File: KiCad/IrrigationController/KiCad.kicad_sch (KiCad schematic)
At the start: 117 parts, among them IC1 MCP23017-E_SO, IC2 MCP23017-E_SO, IC3 DS89C21TMX_NOPB, J1 Screw_Terminal_01x03, J10 Screw_Terminal_01x05, J11 Screw_Terminal_01x02, J12 Screw_Terminal_01x02, J13 Screw_Terminal_01x04, J14 Screw_Terminal_01x02, J15 Screw_Terminal_01x02, J16 Screw_Terminal_01x02, J17 Screw_Terminal_01x02, J18 Screw_Terminal_01x02, J19 Screw_Terminal_01x02, J2 Screw_Terminal_01x03, J20 Conn_01x03_Pin, J21 Screw_Terminal_01x06, J22 Conn_01x04_Pin, J23 Conn_01x05_Pin, J24 Conn_01x06_Pin, J3 Screw_Terminal_01x03, J4 Conn_01x02_Pin, J5 Screw_Terminal_01x03, J6 Screw_Terminal_01x02, J7 Screw_Terminal_01x02, J8 Screw_Terminal_01x02, J9 Screw_Terminal_01x02, K1 2071556-9, K2 2071556-9, Q1 MMBT3906, Q11 MMBT3904, Q12 MMBT3904, Q2 MMBT3906, Q3 MMBT3906, Q6 MMBT3904, Q7 MMBT3904, Q8 MMBT3904, SW1 SW_Push, U1 L298P, U2 ARDUINO_MKR_WAN_1310, U3 L298P, U4 L298P, U5 L298P, U7 L7805

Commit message: Añadido C15 al esquema, que se había esfumado
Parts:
- added C15: 0.1u, Capacitor_SMD:C_1206_3216Metric, symbol Device:C
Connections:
- net +3.3V: now also C15.1
- net Earth: now also C15.2
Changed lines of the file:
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@@
 	)
 	(junction
+		(at 261.62 20.32)
+		(diameter 0)
+		(color 0 0 0 0)
+	)
+	(junction
 		(at 102.87 152.4)
 		(diameter 0)
@@
 	)
 	(junction
+		(at 261.62 27.94)
+		(diameter 0)
+		(color 0 0 0 0)
+	)
+	(junction
 		(at 119.38 185.42)
 		(diameter 0)
@@
 	(wire
 		(pts
+			(xy 254 20.32) (xy 261.62 20.32)
+		)
+		(stroke
+			(width 0)
+			(type default)
+		)
+	)
+	(wire
+		(pts
 			(xy 144.78 152.4) (xy 143.51 152.4)
 		)
@@
 	(wire
 		(pts
+			(xy 254 27.94) (xy 261.62 27.94)
+		)
+		(stroke
+			(width 0)
+			(type default)
+		)
+	)
+	(wire
+		(pts
 			(xy 168.91 149.86) (xy 170.18 149.86)
 		)
@@
 					(unit 1)
 				)
+			)
+		)
+	)
+	(symbol
+		(lib_id "Device:C")
+		(at 254 24.13 0)
+		(unit 1)
+		(exclude_from_sim no)
+		(in_bom yes)
+		(on_board yes)
+		(dnp no)
+		(property "Reference" "C15"
+			(at 256.54 26.67 0)
+			(effects
+				(font
+					(size 1.27 1.27)
+				)
+			)
+		)
+		(property "Value" "0.1u"
+			(at 250.19 21.59 0)
+			(effects
+				(font
+					(size 1.27 1.27)
+				)
+			)
+		)
+		(property "Footprint" "Capacitor_SMD:C_1206_3216Metric"
+			(at 254.9652 27.94 0)
+			(effects
+				(font
+					(size 1.27 1.27)
+				)
+				(hide yes)
+			)
+		)
+		(property "Datasheet" "~"
+			(at 254 24.13 0)
+			(effects
+				(font
+					(size 1.27 1.27)
+				)
+				(hide yes)
+			)
+		)
+		(property "Description" ""
+			(at 254 24.13 0)
+			(effects
+				(font
+					(size 1.27 1.27)
+				)
+				(hide yes)
+			)
+		)
+		(property "Mouser Part Number" "80-C1206X104K1RAUTO"
+			(at 254 24.13 0)
+			(effects
+				(font
+					(size 1.27 1.27)
+				)
+				(hide yes)
+			)
+		)
+		(pin "1"
+		)
+		(pin "2"
+		)
+		(instances
+			(project "KiCad"
+				(path "/557850ac-a946-4dff-8187-8978353577df"
+					(reference "C15")
+					(unit 1)
+				)

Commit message: fixed error on I2C lines
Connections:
- net SCL: now also IC1.12 (SCL), IC2.12 (SCL), J13.2 (Pin_2); no longer IC1.13 (SDA), IC2.13 (SDA), J13.3 (Pin_3)
- net SDA: now also IC1.13 (SDA), IC2.13 (SDA), J13.3 (Pin_3); no longer IC1.12 (SCL), IC2.12 (SCL), J13.2 (Pin_2)
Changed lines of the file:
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@@
 	)
 	(label "SDA"
-		(at 82.55 267.97 0)
+		(at 82.55 270.51 0)
 		(fields_autoplaced yes)
 		(effects
@@
 	)
 	(label "SDA"
-		(at 24.13 267.97 0)
+		(at 24.13 270.51 0)
 		(fields_autoplaced yes)
 		(effects
@@
 	)
 	(label "SCL"
-		(at 369.57 39.37 90)
+		(at 367.03 39.37 90)
 		(fields_autoplaced yes)
 		(effects
@@
 	)
 	(label "SCL"
-		(at 24.13 270.51 0)
+		(at 24.13 267.97 0)
 		(fields_autoplaced yes)
 		(effects
@@
 	)
 	(label "SDA"
-		(at 367.03 39.37 90)
+		(at 369.57 39.37 90)
 		(fields_autoplaced yes)
 		(effects
@@
 	)
 	(label "SCL"
-		(at 82.55 270.51 0)
+		(at 82.55 267.97 0)
 		(fields_autoplaced yes)
 		(effects
@@
 		)
 		(instances
-			(project ""
+			(project "KiCad"
 				(path "/557850ac-a946-4dff-8187-8978353577df"
 					(reference "J20")
@@
 		)
 		(instances
-			(project ""
+			(project "KiCad"
 				(path "/557850ac-a946-4dff-8187-8978353577df"
 					(reference "J23")
@@
 		)
 		(instances
-			(project ""
+			(project "KiCad"
 				(path "/557850ac-a946-4dff-8187-8978353577df"
 					(reference "J24")
@@
 		)
 		(instances
-			(project ""
+			(project "KiCad"
 				(path "/557850ac-a946-4dff-8187-8978353577df"
 					(reference "J4")
@@
 		)
 		(instances
-			(project ""
+			(project "KiCad"
 				(path "/557850ac-a946-4dff-8187-8978353577df"
 					(reference "J22")

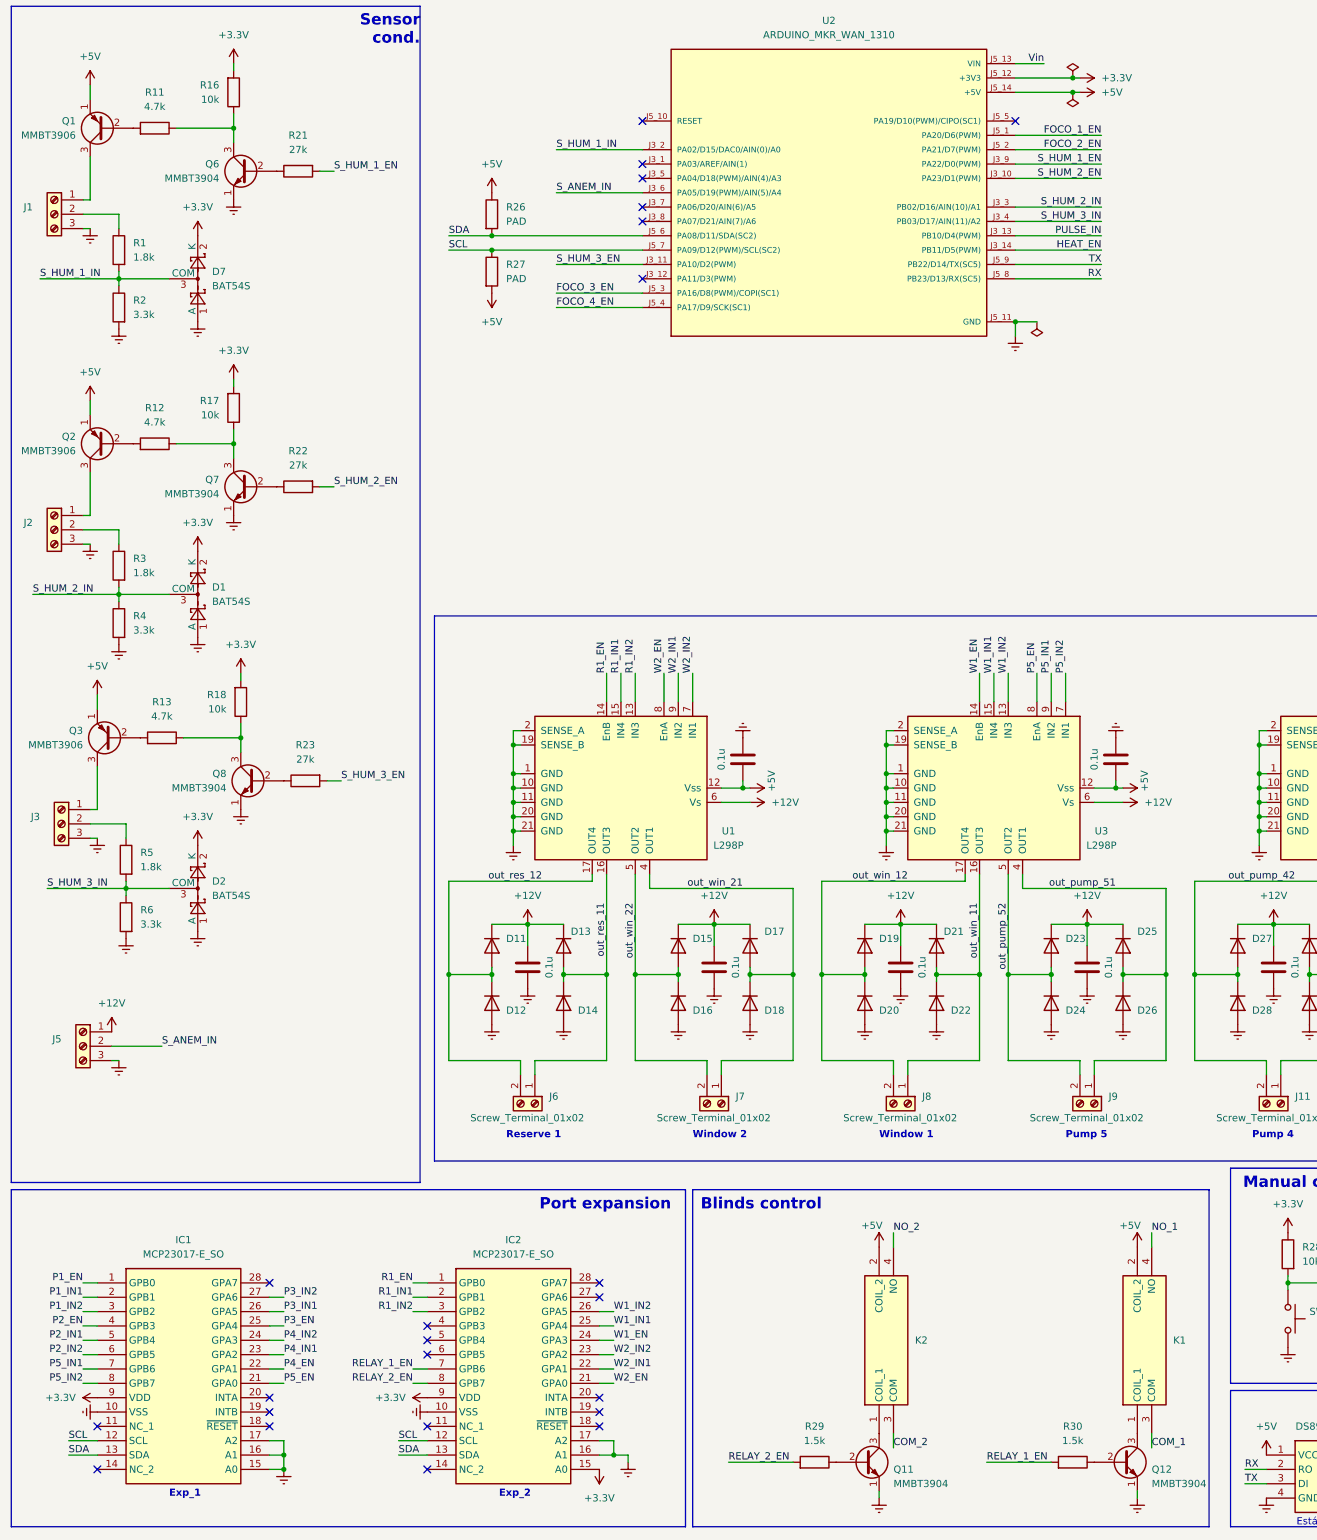
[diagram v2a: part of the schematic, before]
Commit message: Fixed remaining mistakes | wrong transistor + rs422 footprints
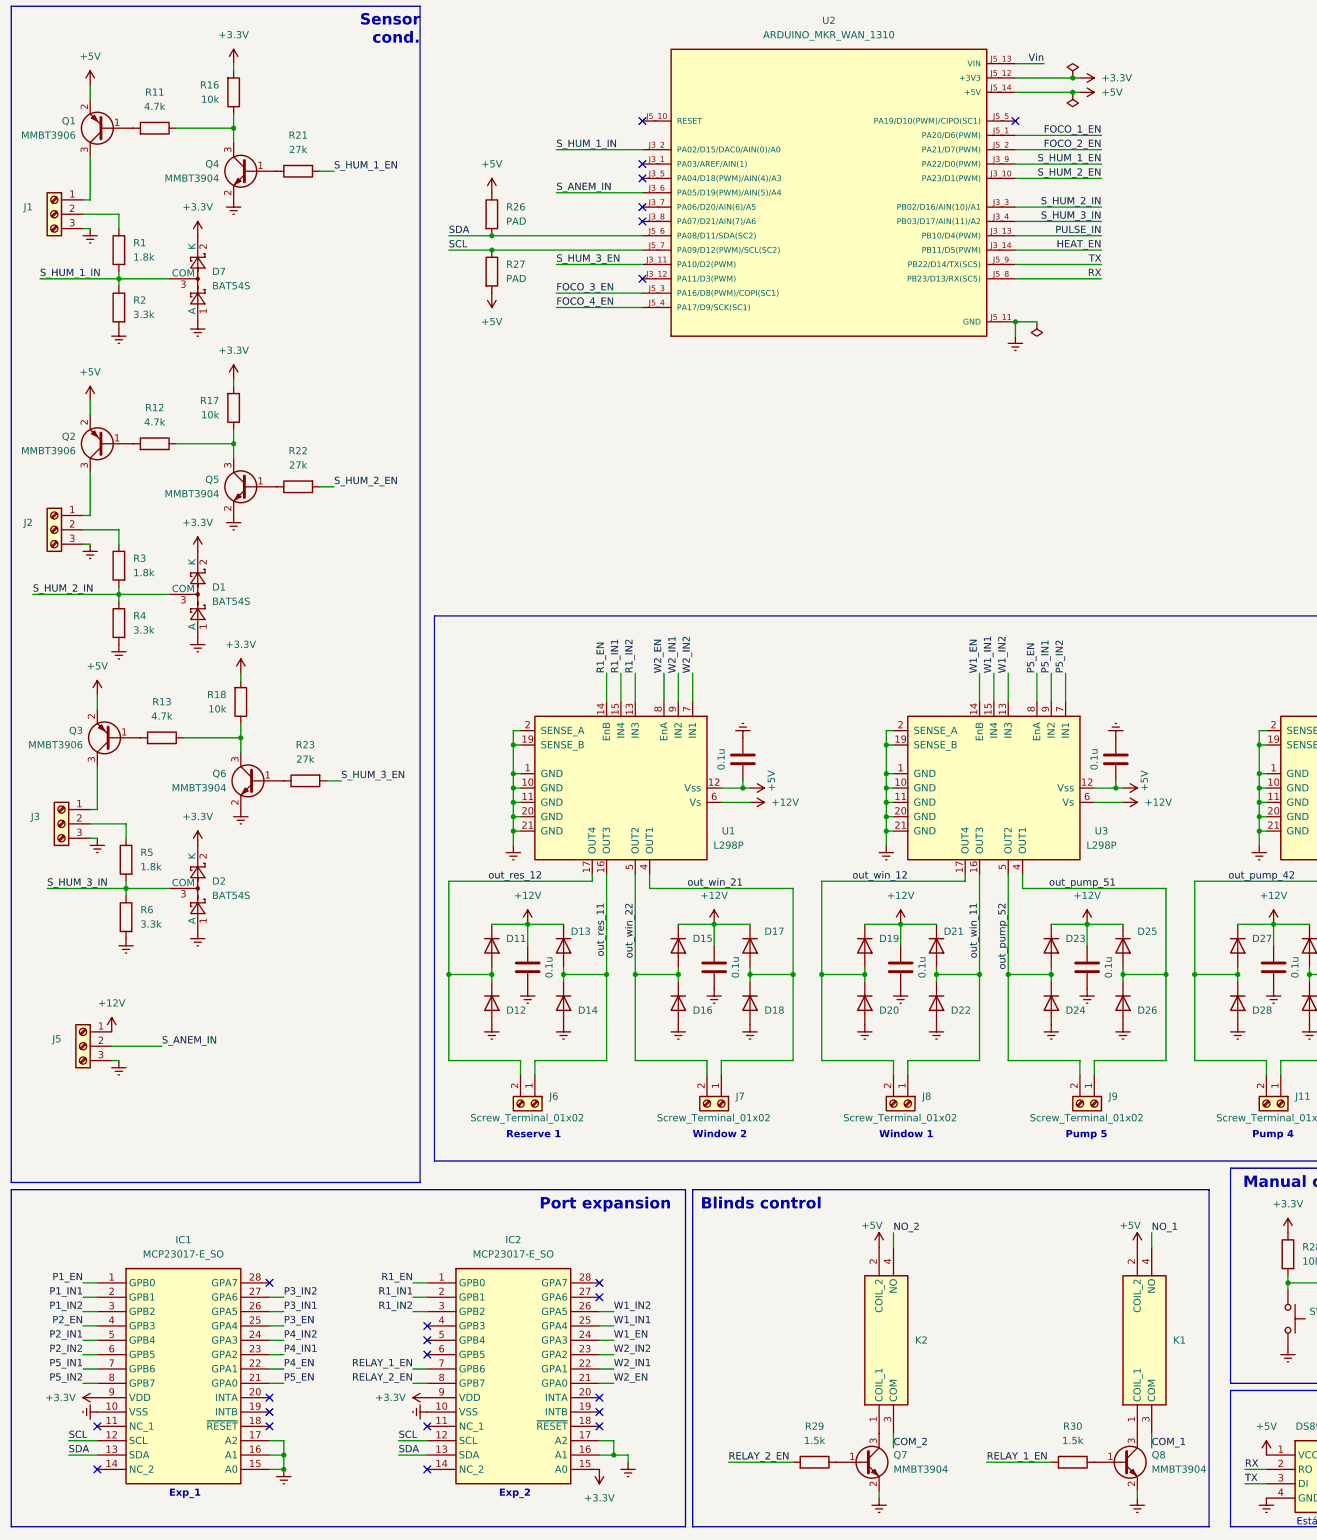
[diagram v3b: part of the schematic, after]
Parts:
- removed Q1, Q2, Q3: MMBT3906, Package_TO_SOT_SMD:SOT-23, symbol Transistor_BJT:2N3906
- removed Q11, Q12, Q6, Q7, Q8: MMBT3904, Package_TO_SOT_SMD:SOT-23, symbol Transistor_BJT:2N3904
- added Q1, Q2, Q3: MMBT3906, Package_TO_SOT_SMD:SOT-23, symbol Transistor_BJT:MMBT3906
- added Q4, Q5, Q6, Q7, Q8: MMBT3904, Package_TO_SOT_SMD:SOT-23, symbol Transistor_BJT:MMBT3904
- IC3: footprint SamacSys_Parts:SOP65P490X110-8N -> SamacSys_Parts:SOIC127P600X175-8N
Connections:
- net +5V: now also Q1.2 (E), Q2.2 (E), Q3.2 (E)
- net Earth: now also Q4.2 (E), Q5.2 (E), Q6.2 (E), Q7.2 (E), Q8.2 (E)
- net at R13.1, R18.1: now also Q6.3 (C)
- net at R13.2: now also Q3.1 (B)
- net at J3.1 (Pin_1): now also Q3.3 (C)
- net at R12.1, R17.1: now also Q5.3 (C)
- net at R11.2: now also Q1.1 (B)
- net at J1.1 (Pin_1): now also Q1.3 (C)
- net at R30.1: now also Q8.1 (B)
- net at R22.1: now also Q5.1 (B)
- net at R21.1: now also Q4.1 (B)
- net at K1.1 (COIL_1): now also Q8.3 (C)
- net at R23.1: now also Q6.1 (B)
- net at R29.1: now also Q7.1 (B)
- net at K2.1 (COIL_1): now also Q7.3 (C)
- net at R11.1, R16.1: now also Q4.3 (C)
- net at R12.2: now also Q2.1 (B)
- net at J2.1 (Pin_1): now also Q2.3 (C)
